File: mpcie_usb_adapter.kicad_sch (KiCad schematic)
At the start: 22 parts, among them J1 USB4105-GF-A, J2 SMA-J-P-H-ST-EM1, J3 SMA-J-P-H-ST-EM1, J4 Conn_Coaxial_Small, J5 Conn_Coaxial_Small, U1 LD1117S33TR, U2 AS-RTK2B-MPCIE-L1L2-F9P-01

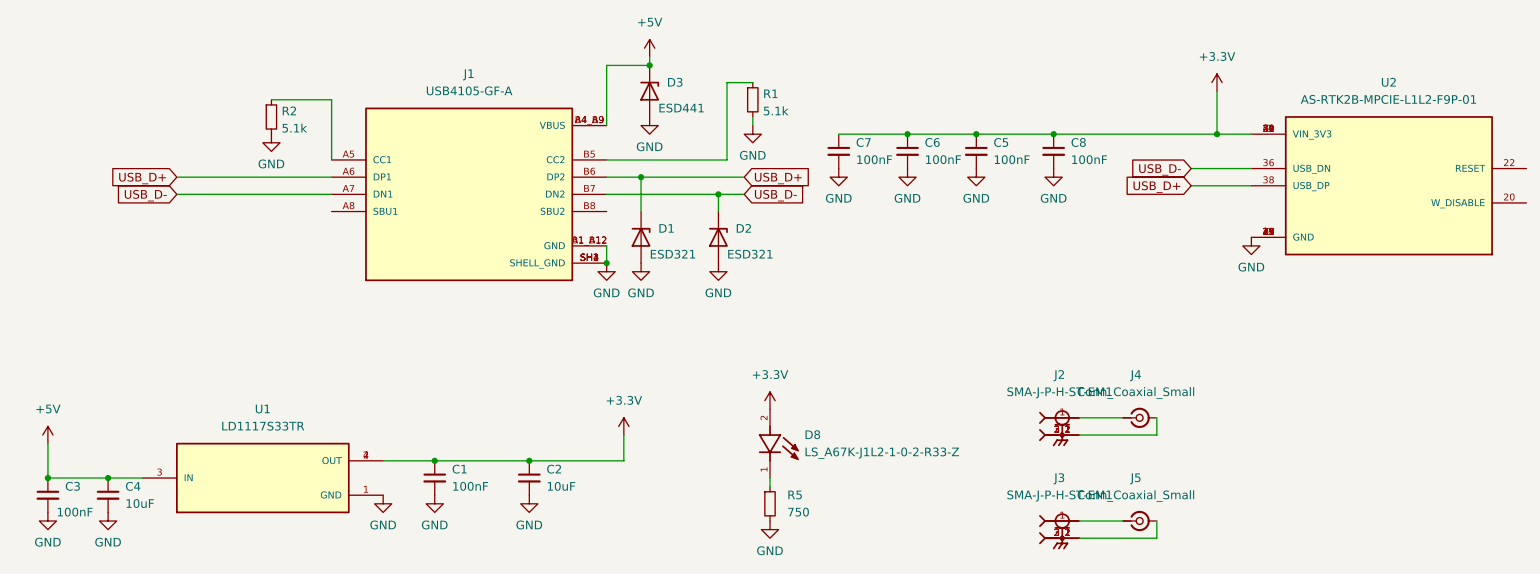
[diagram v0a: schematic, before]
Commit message: integrated updates from Matteo and added 3d models
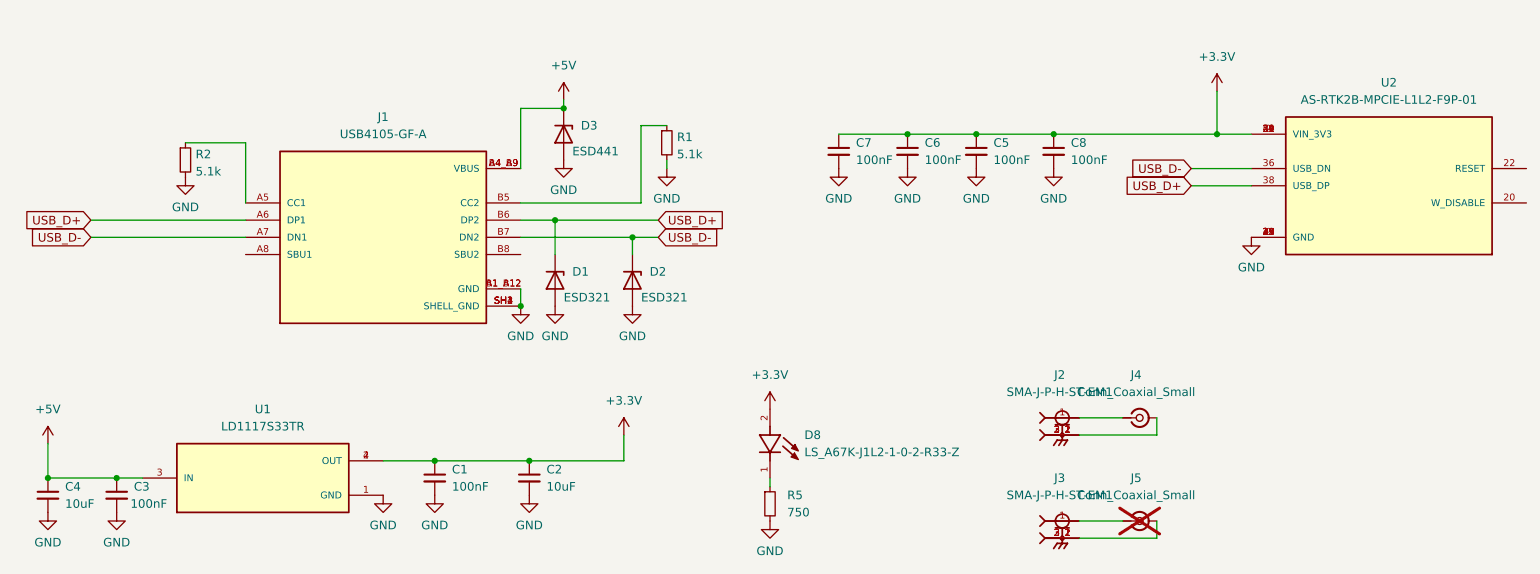
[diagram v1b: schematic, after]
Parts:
- J5: now not fitted
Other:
- moved on the sheet: C3, C4, D1, D2, D3, J1, R1, R2
